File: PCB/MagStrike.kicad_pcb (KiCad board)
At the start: 2 copper layers, 288.7 x 121.5 mm, 72 parts, among them U1 CD74HC4067M, U2 CD74HC4067M, U3 CD74HC4067M, U4 CD74HC4067M

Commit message: more stuff
more silkscreening
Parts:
- added G***: LOGO, github:flagg223432, F.Cu at (196.1, 126.5)
- added G***: LOGO, github:minnnionnn, F.Cu at (132.5, 132.7)
- added G***: LOGO, github:meowmeowmeowe, F.Cu at (148.5, 134.7)
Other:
- board text added: "67"
- board text added: "@2025 Blueprint"
- board text added: "William Gu"

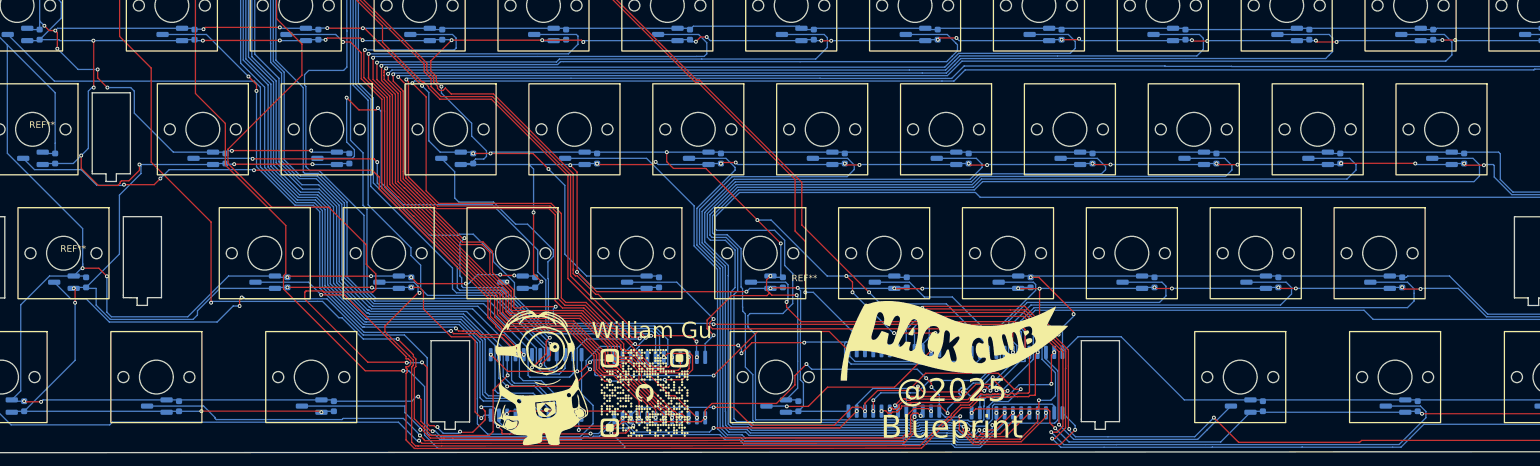
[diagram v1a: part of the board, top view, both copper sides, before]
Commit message: fixed drc issues
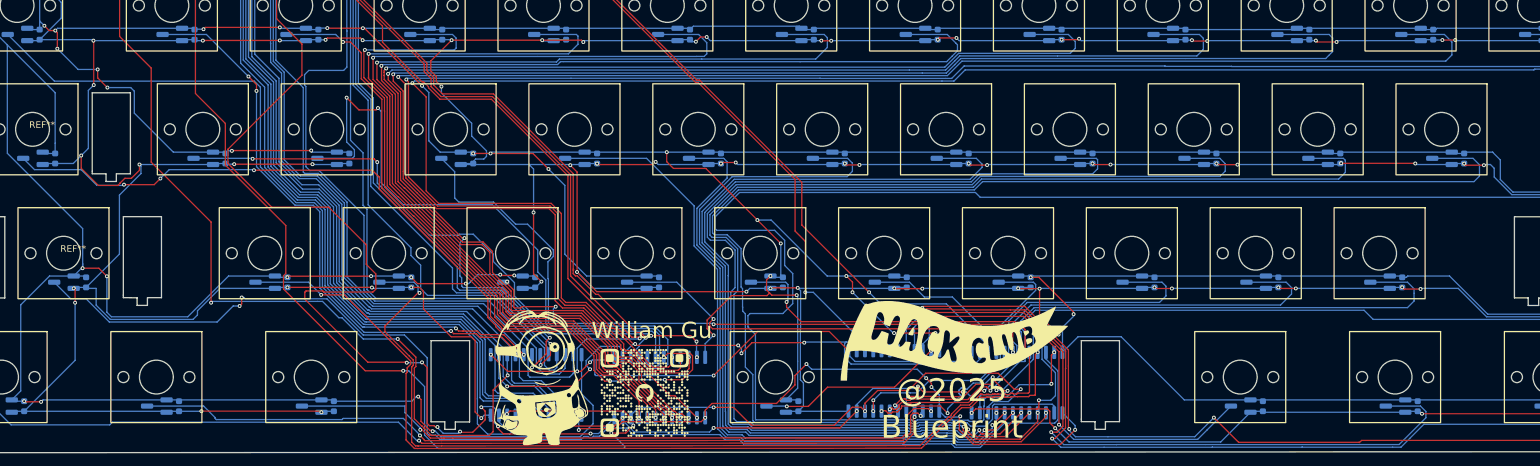
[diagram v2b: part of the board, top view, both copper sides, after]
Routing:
- net SW39: track 197.7 -> 195.0 mm
- net SW37: track 156.0 -> 154.1 mm
- net SW38: track 179.0 -> 177.2 mm
- net SW34: track 98.5 -> 97.3 mm
- net GND: track 1616.9 -> 1616.4 mm
- net SW43: track 149.5 -> 149.0 mm
- net +3V3: track 1635.1 -> 1634.6 mm

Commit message: d
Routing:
- net SW41: track 262.5 -> 259.8 mm
- net SW10: track 235.7 -> 234.3 mm

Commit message: some sad things
i have my pcb but relised i have done the pinout wrong
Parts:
- removed G***: LOGO, github:flagg223432
- removed G***: LOGO, github:minnnionnn
- removed G***: LOGO, github:meowmeowmeowe
- removed the REF** at (305.8, 55.7)
- removed the REF** at (60.5, 112.9)
- removed the REF** at (303.4, 93.8)
- removed the REF** at (298.6, 112.9)
- removed the REF** at (55.7, 93.8)
- added REF**: 2U, Stablilizer:2U, F.Cu at (46.7, 76.0)
- added REF**: TestPoint_Pad_2.0x2.0mm, TestPoint:TestPoint_Pad_2.0x2.0mm, F.Cu at (328.6, 23.1)
- added REF**: 2U, Stablilizer:2U, F.Cu at (51.5, 95.1)
- added REF**: 2U, Stablilizer:2U, F.Cu at (294.4, 76.0)
- added REF**: 2U, Stablilizer:2U, F.Cu at (289.6, 95.1)
- added REF**: 2U, Stablilizer:2U, F.Cu at (296.7, 37.9)
- moved U3 34.4 mm to (176.8, 114.3)
- moved U2 21.6 mm to (140.6, 114.6)
- moved U1 20.4 mm to (122.9, 114.9)
- moved U4 20.1 mm to (195.3, 114.6)
- moved REF** 20.0 mm to (162.7, 99.2)
- moved SW14 20.0 mm to (295.3, 38.1)
- moved SW57 20.0 mm to (159.5, 114.3)
- moved SW58 20.0 mm to (231.0, 114.3)
- moved SW11 20.0 mm to (228.6, 38.1)
- moved SW12 20.0 mm to (247.7, 38.1)
- moved SW17 20.0 mm to (85.7, 57.1)
- moved SW20 20.0 mm to (142.9, 57.1)
- moved SW22 20.0 mm to (181.0, 57.1)
- moved SW24 20.0 mm to (219.1, 57.1)
- moved SW25 20.0 mm to (238.1, 57.1)
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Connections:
- SW1 pad 2: GND -> SW1
- SW1 pad 3: SW1 -> GND
- SW10 pad 2: GND -> SW10
- SW10 pad 3: SW10 -> GND
- SW11 pad 2: GND -> SW11
- SW11 pad 3: SW11 -> GND
- SW12 pad 2: GND -> SW12
- SW12 pad 3: SW12 -> GND
- SW13 pad 2: GND -> SW13
- SW13 pad 3: SW13 -> GND
- SW14 pad 2: GND -> SW14
- SW14 pad 3: SW14 -> GND
- SW15 pad 2: GND -> SW5
- SW15 pad 3: SW15 -> GND
- SW16 pad 2: GND -> SW16
- SW16 pad 3: SW16 -> GND
- SW17 pad 2: GND -> SW17
- SW17 pad 3: SW17 -> GND
- SW18 pad 2: GND -> SW18
- SW18 pad 3: SW18 -> GND
- SW19 pad 2: GND -> SW19
- SW19 pad 3: SW19 -> GND
- SW2 pad 2: GND -> SW2
- SW2 pad 3: SW2 -> GND
- SW20 pad 2: GND -> SW20
- SW20 pad 3: SW20 -> GND
- SW21 pad 2: GND -> SW21
- SW21 pad 3: SW21 -> GND
- SW22 pad 2: GND -> SW22
- SW22 pad 3: SW22 -> GND
- SW23 pad 2: GND -> SW23
- SW23 pad 3: SW23 -> GND
- SW24 pad 2: GND -> SW24
- SW24 pad 3: SW24 -> GND
- SW25 pad 2: GND -> SW25
- SW25 pad 3: SW25 -> GND
- SW26 pad 2: GND -> SW26
- SW26 pad 3: SW26 -> GND
- SW27 pad 2: GND -> SW27
- SW27 pad 3: SW27 -> GND
- SW28 pad 2: GND -> SW28
- SW28 pad 3: SW28 -> GND
- SW29 pad 2: GND -> SW29
- SW29 pad 3: SW29 -> GND
- SW3 pad 2: GND -> SW3
- SW3 pad 3: SW3 -> GND
- SW30 pad 2: GND -> SW30
- SW30 pad 3: SW30 -> GND
- SW31 pad 2: GND -> SW31
- SW31 pad 3: SW31 -> GND
- SW32 pad 2: GND -> SW32
- SW32 pad 3: SW32 -> GND
- SW33 pad 2: GND -> SW33
- SW33 pad 3: SW33 -> GND
- SW34 pad 2: GND -> SW34
- SW34 pad 3: SW34 -> GND
- SW35 pad 2: GND -> SW35
- SW35 pad 3: SW35 -> GND
- SW36 pad 2: GND -> SW36
- SW36 pad 3: SW36 -> GND
- SW37 pad 2: GND -> SW37
- SW37 pad 3: SW37 -> GND
- SW38 pad 2: GND -> SW38
- SW38 pad 3: SW38 -> GND
- SW39 pad 2: GND -> SW39
- SW39 pad 3: SW39 -> GND
- SW4 pad 2: GND -> SW4
- SW4 pad 3: SW4 -> GND
- SW40 pad 2: GND -> SW40
- SW40 pad 3: SW40 -> GND
- SW41 pad 2: GND -> SW41
- SW41 pad 3: SW41 -> GND
- SW42 pad 2: GND -> SW42
- SW42 pad 3: SW42 -> GND
- SW43 pad 2: GND -> SW43
- SW43 pad 3: SW43 -> GND
- SW44 pad 2: GND -> SW44
- SW44 pad 3: SW44 -> GND
- SW45 pad 2: GND -> SW45
- SW45 pad 3: SW45 -> GND
- SW46 pad 2: GND -> SW46
- SW46 pad 3: SW46 -> GND
- SW47 pad 2: GND -> SW47
- SW47 pad 3: SW47 -> GND
- SW48 pad 2: GND -> SW48
- SW48 pad 3: SW48 -> GND
- SW49 pad 2: GND -> SW49
- SW49 pad 3: SW49 -> GND
- SW5 pad 2: GND -> SW5
- SW5 pad 3: SW5 -> GND
- SW50 pad 2: GND -> SW50
- SW50 pad 3: SW50 -> GND
- SW51 pad 2: GND -> SW51
- SW51 pad 3: SW51 -> GND
- SW52 pad 2: GND -> SW52
- SW52 pad 3: SW52 -> GND
- SW53 pad 2: GND -> SW53
- SW53 pad 3: SW53 -> GND
- SW54 pad 2: GND -> SW54
- SW54 pad 3: SW54 -> GND
- SW55 pad 2: GND -> SW55
- SW55 pad 3: SW55 -> GND
- SW56 pad 2: GND -> SW56
- SW56 pad 3: SW56 -> GND
- SW57 pad 2: GND -> SW57
- SW57 pad 3: SW57 -> GND
- SW58 pad 2: GND -> SW58
- SW58 pad 3: SW58 -> GND
- SW59 pad 2: GND -> SW59
- SW59 pad 3: SW59 -> GND
- SW6 pad 2: GND -> SW6
- SW6 pad 3: SW6 -> GND
- SW60 pad 2: GND -> SW60
- SW60 pad 3: SW60 -> GND
- SW61 pad 2: GND -> SW61
- SW61 pad 3: SW61 -> GND
- SW7 pad 2: GND -> SW7
- SW7 pad 3: SW7 -> GND
- SW8 pad 2: GND -> SW8
- SW8 pad 3: SW8 -> GND
- SW9 pad 2: GND -> SW9
- SW9 pad 3: SW9 -> GND
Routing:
- net +3V3: track 1634.6 -> 0.00 mm, vias 39 -> 0
- net GND: track 1616.1 -> 0.00 mm, vias 99 -> 0
- net SW14: track 301.4 -> 0.00 mm, vias 2 -> 0
- net SW28: track 289.9 -> 0.00 mm, vias 2 -> 0
- net SW27: track 270.6 -> 0.00 mm, vias 2 -> 0
- net SW13: track 268.9 -> 0.00 mm, vias 2 -> 0
- net GPI09: track 261.1 -> 0.00 mm, vias 14 -> 0
- net SW41: track 259.8 -> 0.00 mm, vias 2 -> 0
- net GPI08: track 256.1 -> 0.00 mm, vias 9 -> 0
- net SW26: track 255.5 -> 0.00 mm, vias 2 -> 0
- net SW12: track 250.0 -> 0.00 mm
- net SW11: track 240.1 -> 0.00 mm
- net SW25: track 236.7 -> 0.00 mm, vias 5 -> 0
- net SW10: track 234.3 -> 0.00 mm
- net SW9: track 224.7 -> 0.00 mm
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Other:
- board size 288.7 x 121.5 mm -> 105.9 x 13.7 mm
- board text removed: "67"
- board text removed: "@2025 Blueprint"
- board text removed: "William Gu"

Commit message: more stuff
mores stutff
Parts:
- removed REF**: 6U, Stablilizer:6U
- removed REF** (x5): 2U, Stablilizer:2U
- removed REF**: TestPoint_Pad_2.0x2.0mm, TestPoint:TestPoint_Pad_2.0x2.0mm
- moved U1 11.0 mm to (111.9, 114.9)
- moved U4 10.2 mm to (205.5, 113.7)
- moved U3 4.03 mm to (180.8, 114.0)
- moved U2 3.92 mm to (136.7, 114.6)
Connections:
- SW15 pad 2: SW5 -> SW15
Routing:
- net GND: track 0.00 -> 760.1 mm, vias 0 -> 40
- net +3V3: track 0.00 -> 594.9 mm, vias 0 -> 8
- net SW14: track 0.00 -> 322.7 mm, vias 0 -> 2
- net SW13: track 0.00 -> 296.2 mm, vias 0 -> 2
- net SW12: track 0.00 -> 277.8 mm, vias 0 -> 2
- net SW11: track 0.00 -> 258.9 mm, vias 0 -> 2
- net SW10: track 0.00 -> 239.4 mm, vias 0 -> 2
- net GPI08: track 0.00 -> 238.6 mm, vias 0 -> 5
- net GPI09: track 0.00 -> 230.2 mm, vias 0 -> 8
- net SW9: track 0.00 -> 229.8 mm, vias 0 -> 4
- net SW8: track 0.00 -> 213.8 mm, vias 0 -> 4
- net SW28: track 0.00 -> 209.2 mm, vias 0 -> 4
- net SW7: track 0.00 -> 194.7 mm, vias 0 -> 2
- net SW27: track 0.00 -> 183.9 mm, vias 0 -> 4
- net SW6: track 0.00 -> 173.7 mm, vias 0 -> 2
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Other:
- board size 105.9 x 13.7 mm -> 284.7 x 121.6 mm

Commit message: push final 1.2
This is the mabe final version for my thing it should be done i will do some final checks tho
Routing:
- net GND: track 760.1 -> 1767.6 mm, vias 40 -> 95
- net +3V3: track 594.9 -> 1402.0 mm, vias 8 -> 48
- net GPI014: track 0.00 -> 179.8 mm, vias 0 -> 5
- net SW54: track 0.00 -> 176.4 mm, vias 0 -> 2
- net GPIO15: track 0.00 -> 170.3 mm, vias 0 -> 3
- net SW55: track 0.00 -> 151.7 mm, vias 0 -> 2
- net SW42: track 0.00 -> 145.0 mm, vias 0 -> 2
- net SW41: track 0.00 -> 142.6 mm, vias 0 -> 4
- net GPI013: track 0.00 -> 130.2 mm, vias 0 -> 3
- net SW56: track 0.00 -> 129.8 mm, vias 0 -> 2
- net GPI010: track 114.4 -> 236.5 mm, vias 4 -> 10
- net GPI012: track 0.00 -> 118.6 mm, vias 0 -> 6
- net SW40: track 0.00 -> 117.9 mm, vias 0 -> 2
- net GPI011: track 109.7 -> 227.4 mm, vias 0 -> 4
- net SW43: track 0.00 -> 116.0 mm, vias 0 -> 2
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
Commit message: final stuff with silkscreen
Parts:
- added G***: LOGO, LOGO, F.Cu at (119.1, 116.5)
- added G***: LOGO, LOGO, F.Cu at (136.2, 117.3)
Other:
- board text added: "Made for Blueprint @ Hackclub 2025"
- board text added: "William Gu"

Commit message: idk what i did
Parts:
- moved G*** 17.6 mm to (119.8, 134.1)
- moved U1 17.6 mm to (112.6, 132.5)
- moved U2 17.6 mm to (137.4, 132.2)
- moved U4 17.6 mm to (206.2, 131.2)
- moved SW24 17.6 mm to (219.7, 74.7)
- moved SW15 17.6 mm to (43.5, 74.7)
- moved SW16 17.6 mm to (67.3, 74.7)
- moved SW17 17.6 mm to (86.4, 74.7)
- moved SW18 17.6 mm to (105.4, 74.7)
- moved SW19 17.6 mm to (124.5, 74.7)
- moved SW20 17.6 mm to (143.5, 74.7)
- moved SW21 17.6 mm to (162.6, 74.7)
- moved SW22 17.6 mm to (181.6, 74.7)
- moved SW23 17.6 mm to (200.7, 74.7)
- moved SW25 17.6 mm to (238.8, 74.7)
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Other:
- board size 284.7 x 121.6 mm -> 284.7 x 121.7 mm
